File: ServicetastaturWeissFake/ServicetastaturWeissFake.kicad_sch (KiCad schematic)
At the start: 68 parts, among them J1 Automat, SW1 Gewinn, SW10 Lautspr./, SW11 ↓0,10, SW12 ↑0,10, SW13 ↓Serie, SW14 ↑Serie, SW15 Zeit, SW16 ↑1,-, SW17 ↙0,10, SW18 ↙1,-, SW19 Auszahlquote, SW2 Foul, SW20 ↙5,-, SW21 Münzsp., SW22 Sp.Zähl, SW23 Lampen, SW24 Reset, SW25 Initialisieren, SW26 Münzung, SW27 Ende, SW28 ↑0,10, SW29 ↓Serie, SW3 ↙2,-, SW30 ↑Serie, SW31 ↓1,-, SW32 ↑1,-, SW4 HW-Test, SW5 Münzsp., SW6 Sp.Zähl, SW7 Dauerlauf, SW8 Reset, SW9 Initialisieren, U1 CC56-12CGKWA, U2 CC56-12CGKWA, U3 74LS48, U4 74LS145, U5 74LS48, U6 74LS145

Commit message: schaltplan
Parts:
- removed D4: LED, LED_SMD:LED_0805_2012Metric, symbol Device:LED
- removed R1, R2, R3, R4, R5, R6, R7, R8, R9: 470 Ω, Resistor_THT:R_Axial_DIN0207_L6.3mm_D2.5mm_P7.62mm_Horizontal, symbol Device:R
- removed U3: 74LS48, Package_DIP:DIP-16_W7.62mm, symbol 74xx:74LS48
- removed U4: 74LS145, Package_DIP:DIP-16_W7.62mm, symbol 74xx:74LS145
- added C5, C6: 1000pF, Capacitor_SMD:C_0603_1608Metric, symbol Device:C
- added F1: Fuse, Fuse:Fuse_0805_2012Metric, symbol Device:Fuse
- added JP2: Geschwindigkeit, Jumper:SolderJumper-3_P1.3mm_Bridged12_Pad1.0x1.5mm, symbol Jumper:Jumper_3_Bridged12
- added R19, R20: 180 kΩ, Resistor_SMD:R_0603_1608Metric, symbol Device:R
- added SW33, SW34, SW35, SW36, SW37, SW38, SW39, SW40, SW41, SW42, SW43, SW44, SW45, SW46, SW47, SW48: SW_Push_LED, symbol Switch:SW_Push_LED
- added U3: 74LS08, Package_SO:SOIC-14_3.9x8.7mm_P1.27mm, symbol 74xx:74LS08
- added U4: 4017, Package_SO:SOP-16_3.9x9.9mm_P1.27mm, symbol 4xxx:4017
- added U7: HEF4093B, Package_SO:SOIC-14_3.9x8.7mm_P1.27mm, symbol 4xxx:HEF4093B
- C3, C4: footprint Capacitor_SMD:C_0805_2012Metric -> Capacitor_SMD:C_0603_1608Metric
- JP1: value Jumper_3_Bridged12 -> Invers; footprint Jumper:SolderJumper-3_P1.3mm_Bridged12_Pad1.0x1.5mm_NumberLabels -> Jumper:SolderJumper-3_P1.3mm_Bridged12_Pad1.0x1.5mm
- R10, R11, R12, R13, R14, R15, R16, R18: footprint Resistor_SMD:R_0805_2012Metric -> Resistor_SMD:R_0603_1608Metric
- R17: footprint Resistor_SMD:R_0805_2012Metric -> Resistor_SMD:R_0603_1608Metric; now fitted
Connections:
- net +5V: now also F1.2, R20.2, U3.14 (VCC), U4.16 (VDD), U7.14 (VCC); no longer J1.2 (Pin_2), JP1.3 (B), R17.1
- net A0: now also U3.5
- net A1: now also U3.1
- net A2: now also U3.4
- net A3: now also U3.9
- net GND: now also R19.1, SW33.3 (K), SW34.3 (K), SW35.3 (K), SW37.3 (K), SW38.3 (K), SW39.3 (K), SW40.3 (K), SW41.3 (K), SW42.3 (K), SW43.3 (K), SW44.3 (K), SW45.3 (K), SW46.3 (K), SW47.3 (K), SW48.3 (K), U3.7 (GND), U4.13 (CKEN), U4.15 (Reset), U4.8 (VSS), U7.7 (GND)
- net S0: now also U7.1, U7.2
- net S2: now also JP2.3 (B)
- net S3: now also JP2.1 (A)
- net TS0: now also SW40.1, SW48.1
- net TS1: now also SW39.1, SW47.1
- net TS2: now also SW38.1, SW46.1
- net TS3: now also SW37.1, SW45.1
- net TS4: now also SW36.1, SW44.1
- net TS5: now also SW35.1, SW43.1
- net TS6: now also SW34.1, SW42.1
- net TS7: now also SW33.1, SW41.1
- net at D1.1 (K), SW10.1, SW11.1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: now also SW41.2, SW42.2, SW43.2, SW44.2, SW45.2, SW46.2, SW47.2, SW48.2
- net at U1.3 (DPX), U2.3 (DPX): now also R17.2
- net at D2.1 (K), SW1.1, SW17.1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: now also SW33.2, SW34.2, SW35.2, SW36.2, SW37.2, SW38.2, SW39.2, SW40.2
- new net: U7.10, U7.12
- new net: C5.2, R19.2, U7.8, U7.9
- new net: R17.1, U3.8
- new net: U3.2, U3.6
- new net: U3.10, U3.3
- new net: JP1.1 (A), U7.4
- new net: JP1.3 (B), U7.11, U7.5, U7.6
- new net: C6.2, R20.1, U7.13
- new net: F1.1, J1.2 (Pin_2)
- new net: JP2.2 (C), U4.14 (CLK)
- new net: C5.1, C6.1, U7.3
- new net LED0: U4.3 (Q0)
- new net LED1: SW33.4 (A), SW48.4 (A), U4.2 (Q1)
- new net LED2: SW34.4 (A), SW47.4 (A), U4.4 (Q2)
- new net LED3: SW35.4 (A), SW46.4 (A), U4.7 (Q3)
- new net LED4: SW36.4 (A), SW45.4 (A), U4.10 (Q4)
- new net LED5: SW37.4 (A), SW44.4 (A), U4.1 (Q5)
- new net LED6: SW38.4 (A), SW43.4 (A), U4.5 (Q6)
- new net LED7: SW39.4 (A), SW42.4 (A), U4.6 (Q7)
- new net LED8: SW40.4 (A), SW41.4 (A), U4.9 (Q8)
- new net LED9: U4.11 (Q9)
- now unconnected: U6.10 (Q8), U6.11 (Q9)
- no-connect marks 1 -> 6
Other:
- moved on the sheet: C1, C2, C3, C4, D1, D2, D3, H1, H2, J1, R10, R11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

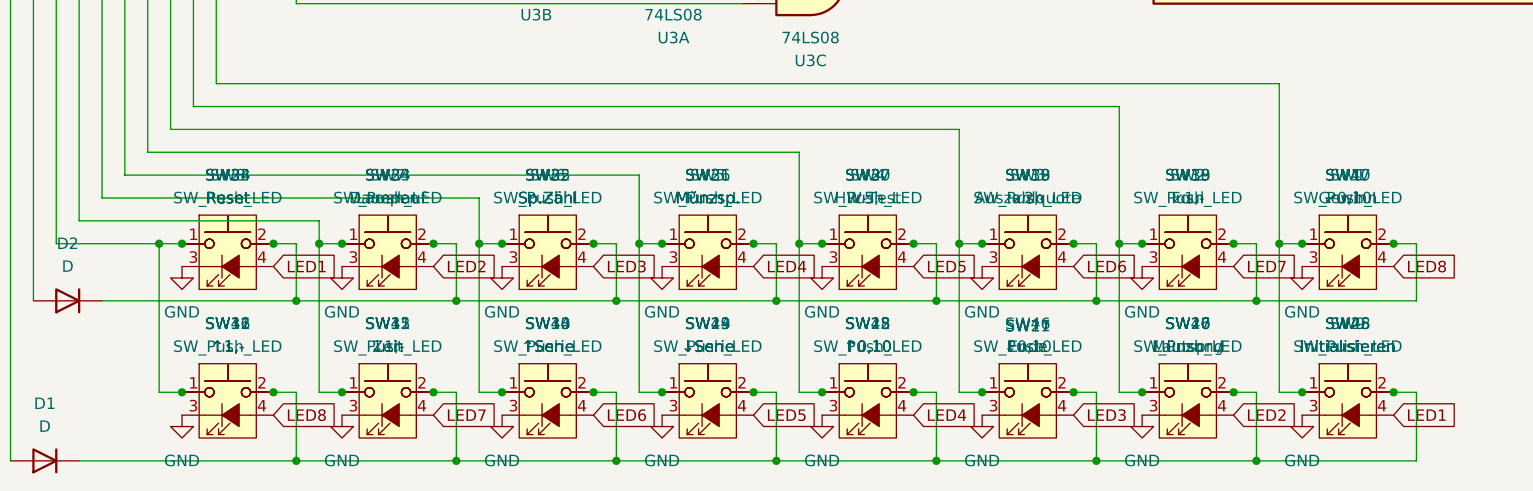
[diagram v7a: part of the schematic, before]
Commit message: more buttons
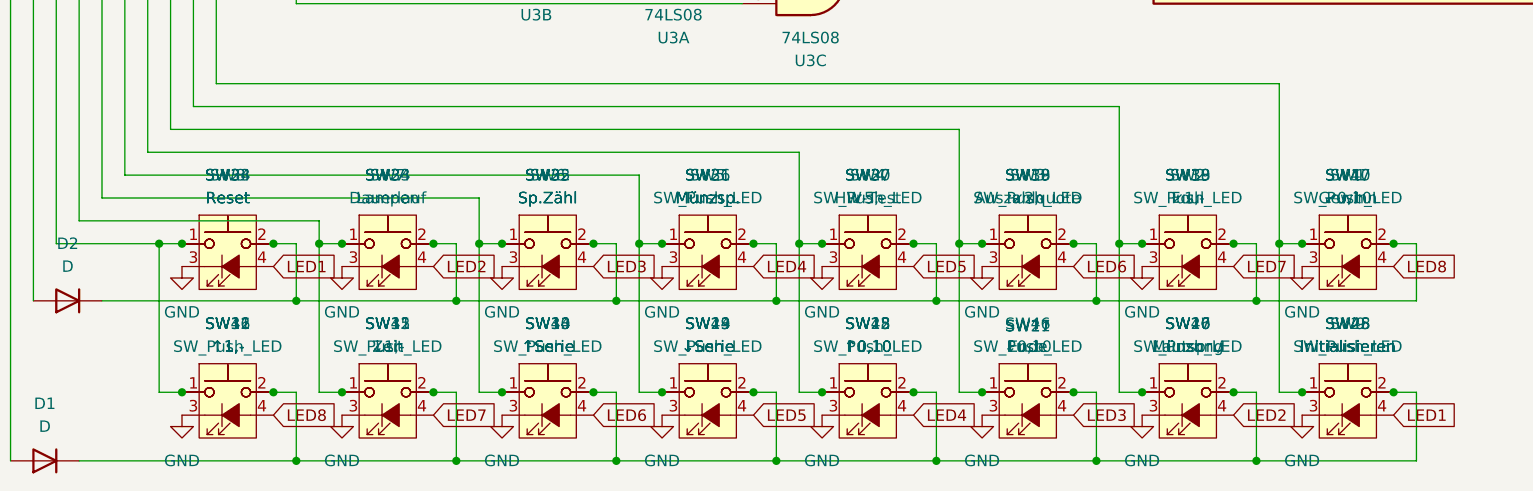
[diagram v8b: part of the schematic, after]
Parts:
- SW33, SW34, SW35, SW36, SW37, SW38, SW39, SW40, SW41, SW42, SW43, SW44, SW45, SW46, SW47, SW48: footprint (none) -> ChinaButton:TS12
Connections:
- net GND: now also SW36.3 (K)
- net TS0: now also SW1.1, SW17.1, SW25.1, SW9.1; no longer SW1.2, SW17.2, SW25.2, SW9.2
- net TS1: now also SW10.1, SW18.1, SW2.1, SW26.1; no longer SW10.2, SW18.2, SW2.2, SW26.2
- net TS2: now also SW11.1, SW19.1, SW27.1, SW3.1; no longer SW11.2, SW19.2, SW27.2, SW3.2
- net TS3: now also SW12.1, SW20.1, SW28.1, SW4.1; no longer SW12.2, SW20.2, SW28.2, SW4.2
- net TS4: now also SW13.1, SW21.1, SW29.1, SW5.1; no longer SW13.2, SW21.2, SW29.2, SW5.2
- net TS5: now also SW14.1, SW22.1, SW30.1, SW6.1; no longer SW14.2, SW22.2, SW30.2, SW6.2
- net TS6: now also SW15.1, SW23.1, SW31.1, SW7.1; no longer SW15.2, SW23.2, SW31.2, SW7.2
- net TS7: now also SW16.1, SW24.1, SW32.1, SW8.1; no longer SW16.2, SW24.2, SW32.2, SW8.2
- new net: D1.1 (K), SW10.2, SW11.2, SW12.2, SW13.2, SW14.2, SW15.2, SW16.2, SW25.2, SW26.2, SW27.2, SW28.2, SW29.2, SW30.2, SW31.2, SW32.2, SW41.2, SW42.2, SW43.2, SW44.2, SW45.2, SW46.2, SW47.2, SW48.2, SW9.2
- new net: D2.1 (K), SW1.2, SW17.2, SW18.2, SW19.2, SW2.2, SW20.2, SW21.2, SW22.2, SW23.2, SW24.2, SW3.2, SW33.2, SW34.2, SW35.2, SW36.2, SW37.2, SW38.2, SW39.2, SW4.2, SW40.2, SW5.2, SW6.2, SW7.2, SW8.2
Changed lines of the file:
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@@
 		(lib_id "Switch:SW_Push")
 		(at 93.98 185.42 0)
-		(mirror y)
 		(unit 1)
 		(exclude_from_sim no)
@@
 		(lib_id "Switch:SW_Push")
 		(at 76.2 185.42 0)
-		(mirror y)
 		(unit 1)
 		(exclude_from_sim no)
@@
 		(lib_id "Switch:SW_Push")
 		(at 129.54 185.42 0)
-		(mirror y)
 		(unit 1)
 		(exclude_from_sim no)
@@
 		(lib_id "Switch:SW_Push")
 		(at 129.54 185.42 0)
-		(mirror y)
 		(unit 1)
 		(exclude_from_sim no)
@@
 		(lib_id "Switch:SW_Push")
 		(at 111.76 168.91 0)
-		(mirror y)
 		(unit 1)
 		(exclude_from_sim no)
@@
 			)
 		)
-		(property "Footprint" ""
+		(property "Footprint" "ChinaButton:TS12"
 			(at 129.54 163.83 0)
 			(effects
@@
 		(lib_id "Switch:SW_Push")
 		(at 165.1 185.42 0)
-		(mirror y)
 		(unit 1)
 		(exclude_from_sim no)
@@
 		(lib_id "Switch:SW_Push")
 		(at 147.32 168.91 0)
-		(mirror y)
 		(unit 1)
 		(exclude_from_sim no)
@@
 					(size 1.27 1.27)
 				)
+				(hide yes)
 			)
 		)
-		(property "Footprint" ""
+		(property "Footprint" "ChinaButton:TS12"
 			(at 58.42 163.83 0)
 			(effects
@@
 		(lib_id "Switch:SW_Push")
 		(at 93.98 168.91 0)
-		(mirror y)
 		(unit 1)
 		(exclude_from_sim no)
@@
 			)
 		)
-		(property "Footprint" ""
+		(property "Footprint" "ChinaButton:TS12"
 			(at 111.76 163.83 0)
 			(effects
@@
 		(lib_id "Switch:SW_Push")
 		(at 76.2 168.91 0)
-		(mirror y)
 		(unit 1)
 		(exclude_from_sim no)
@@
 			)
 		)
-		(property "Footprint" ""
+		(property "Footprint" "ChinaButton:TS12"
 			(at 147.32 163.83 0)
 			(effects
@@
 		(lib_id "Switch:SW_Push")
 		(at 165.1 168.91 0)
-		(mirror y)
 		(unit 1)
 		(exclude_from_sim no)
@@
 			)
 		)
-		(property "Footprint" ""
+		(property "Footprint" "ChinaButton:TS12"
 			(at 40.64 180.34 0)
 			(effects
@@
 		(lib_id "Switch:SW_Push")
 		(at 129.54 168.91 0)
-		(mirror y)
 		(unit 1)
 		(exclude_from_sim no)
@@
 		(lib_id "Switch:SW_Push")
 		(at 129.54 168.91 0)
-		(mirror y)
 		(unit 1)
 		(exclude_from_sim no)
@@
 		(lib_id "Switch:SW_Push")
 		(at 165.1 185.42 0)
-		(mirror y)
 		(unit 1)
 		(exclude_from_sim no)
@@
 		(lib_id "Switch:SW_Push")
 		(at 58.42 168.91 0)
-		(mirror y)
 		(unit 1)
 		(exclude_from_sim no)
@@
 		(on_board yes)
 		(dnp no)
-		(fields_autoplaced yes)
 		(property "Reference" "SW7"
 			(at 58.42 161.29 0)
@@
 			)
 		)
-		(property "Footprint" ""
+		(property "Footprint" "ChinaButton:TS12"
 			(at 129.54 180.34 0)
 			(effects
@@
 		(lib_id "Switch:SW_Push")
 		(at 93.98 185.42 0)
-		(mirror y)
 		(unit 1)
 		(exclude_from_sim no)
@@
 					(size 1.27 1.27)
 				)
+				(hide yes)
 			)
 		)
-		(property "Footprint" ""
+		(property "Footprint" "ChinaButton:TS12"
 			(at 76.2 163.83 0)
 			(effects
@@
 		(lib_id "Switch:SW_Push")
 		(at 111.76 185.42 0)
-		(mirror y)
 		(unit 1)
 		(exclude_from_sim no)
@@
 		(lib_id "Switch:SW_Push")
 		(at 111.76 168.91 0)
-		(mirror y)
 		(unit 1)
 		(exclude_from_sim no)
@@
 			)
 		)
-		(property "Footprint" ""
+		(property "Footprint" "ChinaButton:TS12"
 			(at 76.2 180.34 0)
 			(effects
@@
 			)
 		)
-		(property "Footprint" ""
+		(property "Footprint" "ChinaButton:TS12"
 			(at 93.98 163.83 0)
 			(effects
@@
 		(lib_id "Switch:SW_Push")
 		(at 147.32 168.91 0)
-		(mirror y)
 		(unit 1)
 		(exclude_from_sim no)
@@
 	(symbol
 		(lib_id "power:GND")
-		(at 88.9 171.4439 0)
+		(at 88.9 171.45 0)
 		(unit 1)
 		(exclude_from_sim no)
@@
 		(fields_autoplaced yes)
 		(property "Reference" "#PWR032"
-			(at 88.9 177.7939 0)
+			(at 88.9 177.8 0)
 			(effects
 				(font
@@
 		)
 		(property "Value" "GND"
-			(at 88.9 176.53 0)
+			(at 88.9 176.5361 0)
 			(effects
 				(font
@@
 		)
 		(property "Footprint" ""
-			(at 88.9 171.4439 0)
+			(at 88.9 171.45 0)
 			(effects
 				(font
@@
 		)
 		(property "Datasheet" ""
-			(at 88.9 171.4439 0)
+			(at 88.9 171.45 0)
 			(effects
 				(font
@@
 		)
 		(property "Description" "Power symbol creates a global label with name \"GND\" , ground"
-			(at 88.9 171.4439 0)
+			(at 88.9 171.45 0)
 			(effects
 				(font
@@
 		(lib_id "Switch:SW_Push")
 		(at 76.2 168.91 0)
-		(mirror y)
 		(unit 1)
 		(exclude_from_sim no)
@@
 		(lib_id "Switch:SW_Push")
 		(at 147.32 185.42 0)
-		(mirror y)
 		(unit 1)
 		(exclude_from_sim no)
@@
 			)
 		)
-		(property "Footprint" ""
+		(property "Footprint" "ChinaButton:TS12"
 			(at 147.32 180.34 0)
 			(effects
@@
 			)
 		)
-		(property "Footprint" ""
+		(property "Footprint" "ChinaButton:TS12"
 			(at 93.98 180.34 0)
 			(effects
@@
 			)
 		)
-		(property "Footprint" ""
+		(property "Footprint" "ChinaButton:TS12"
 			(at 165.1 180.34 0)
 			(effects
@@
 		(lib_id "Switch:SW_Push")
 		(at 58.42 168.91 0)
-		(mirror y)
 		(unit 1)
 		(exclude_from_sim no)
@@
 		(on_board yes)
 		(dnp no)
-		(fields_autoplaced yes)
 		(property "Reference" "SW23"
 			(at 58.42 161.29 0)
@@
 			)
 		)
-		(property "Footprint" ""
+		(property "Footprint" "ChinaButton:TS12"
 			(at 165.1 163.83 0)
 			(effects
@@
 		(lib_id "Switch:SW_Push")
 		(at 111.76 185.42 0)
-		(mirror y)
 		(unit 1)
 		(exclude_from_sim no)
@@
 					(size 1.27 1.27)
 				)
+				(hide yes)
 			)
 		)
-		(property "Footprint" ""
+		(property "Footprint" "ChinaButton:TS12"
 			(at 40.64 163.83 0)
 			(effects
@@
 		(lib_id "Switch:SW_Push")
 		(at 147.32 185.42 0)
-		(mirror y)
 		(unit 1)
 		(exclude_from_sim no)
@@
 		(lib_id "Switch:SW_Push")
 		(at 40.64 168.91 0)
-		(mirror y)
 		(unit 1)
 		(exclude_from_sim no)
@@
 		(on_board yes)
 		(dnp no)
-		(fields_autoplaced yes)
 		(property "Reference" "SW8"
 			(at 40.64 161.29 0)
@@
 		(lib_id "Switch:SW_Push")
 		(at 58.42 185.42 0)
-		(mirror y)
 		(unit 1)
 		(exclude_from_sim no)
@@
 		(lib_id "Switch:SW_Push")
 		(at 76.2 185.42 0)
-		(mirror y)
 		(unit 1)
 		(exclude_from_sim no)
@@
 		(lib_id "Switch:SW_Push")
 		(at 40.64 168.91 0)
-		(mirror y)
 		(unit 1)
 		(exclude_from_sim no)
@@
 		(on_board yes)
 		(dnp no)
-		(fields_autoplaced yes)
 		(property "Reference" "SW24"
 			(at 40.64 161.29 0)
@@
 			)
 		)
-		(property "Footprint" ""
+		(property "Footprint" "ChinaButton:TS12"
 			(at 58.42 180.34 0)
 			(effects
@@
 		(lib_id "Switch:SW_Push")
 		(at 58.42 185.42 0)
-		(mirror y)
 		(unit 1)
 		(exclude_from_sim no)
@@
 		(lib_id "Switch:SW_Push")
 		(at 40.64 185.42 0)
-		(mirror y)
 		(unit 1)
 		(exclude_from_sim no)
@@
 		(lib_id "Switch:SW_Push")
 		(at 165.1 168.91 0)
-		(mirror y)
 		(unit 1)
 		(exclude_from_sim no)
@@
 		(lib_id "Switch:SW_Push")
 		(at 93.98 168.91 0)
-		(mirror y)
 		(unit 1)
 		(exclude_from_sim no)
@@
 			)
 		)
-		(property "Footprint" ""
+		(property "Footprint" "ChinaButton:TS12"
 			(at 111.76 180.34 0)
 			(effects
@@
 		(lib_id "Switch:SW_Push")
 		(at 40.64 185.42 0)
-		(mirror y)
 		(unit 1)
 		(exclude_from_sim no)
